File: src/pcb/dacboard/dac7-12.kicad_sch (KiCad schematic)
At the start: 18 parts, among them U22 AD8676xR, U23 AD8676xR, U24 AD8676xR, U25 AD8676xR, U26 AD5791BRUZ, U27 AD5791BRUZ, U28 AD5791BRUZ, U29 AD5791BRUZ, U30 AD8676xR, U31 AD8676xR, U32 AD5791BRUZ, U33 AD5791BRUZ

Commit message: dacboard routing
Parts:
- C28, C29, C30, C31, C32, C33: footprint (none) -> Capacitor_SMD:C_0603_1608Metric_Pad1.08x0.95mm_HandSolder
- U26, U27, U28, U29, U32, U33: footprint RU_20_ADI -> Package_SO:TSSOP-20_4.4x6.5mm_P0.65mm

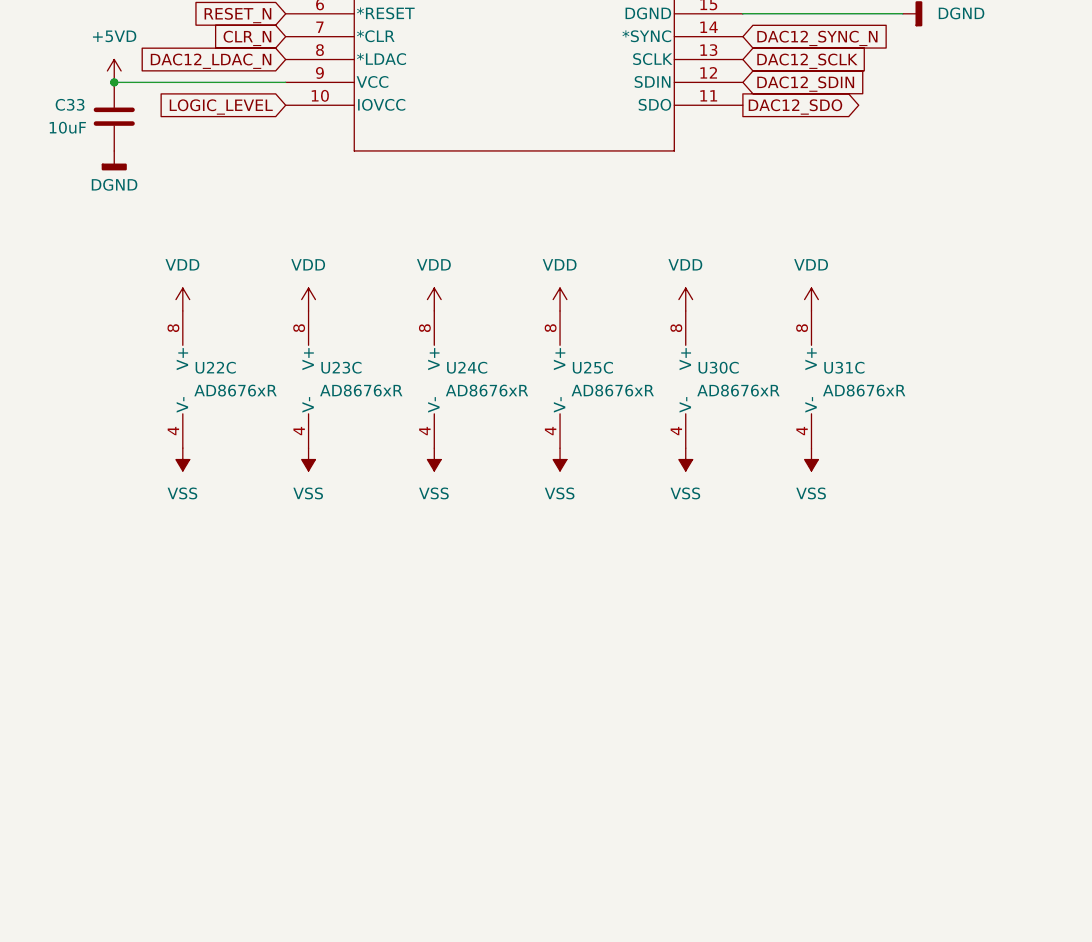
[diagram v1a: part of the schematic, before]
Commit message: adding more capacitors to analog side
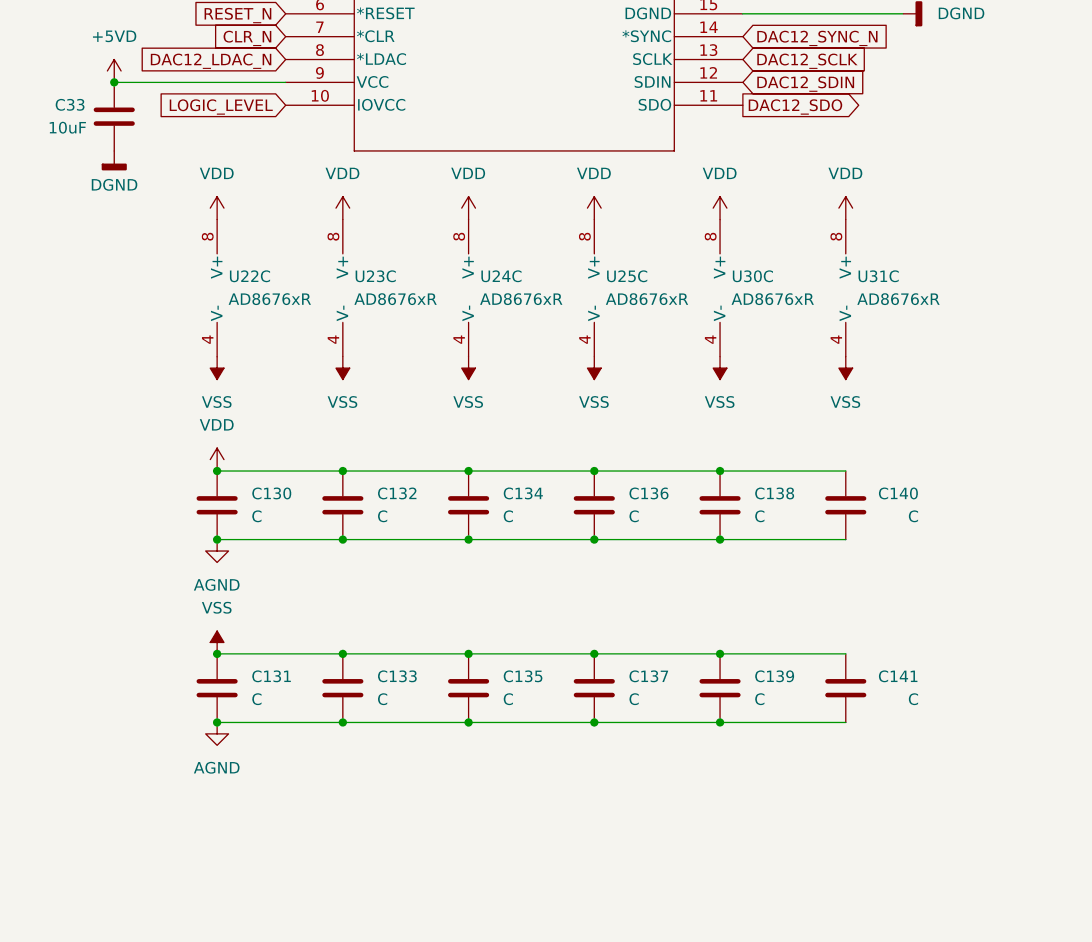
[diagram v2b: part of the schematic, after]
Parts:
- added C130, C131, C132, C133, C134, C135, C136, C137, C138, C139, C140, C141: C, Capacitor_SMD:C_0402_1005Metric_Pad0.74x0.62mm_HandSolder, symbol Device:C
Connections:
- net AGND: now also C130.2, C131.2, C132.2, C133.2, C134.2, C135.2, C136.2, C137.2, C138.2, C139.2, C140.2, C141.2
- net VDD: now also C130.1, C132.1, C134.1, C136.1, C138.1, C140.1
- net VSS: now also C131.1, C133.1, C135.1, C137.1, C139.1, C141.1
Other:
- moved on the sheet: U22C, U23C, U24C, U25C, U30C, U31C

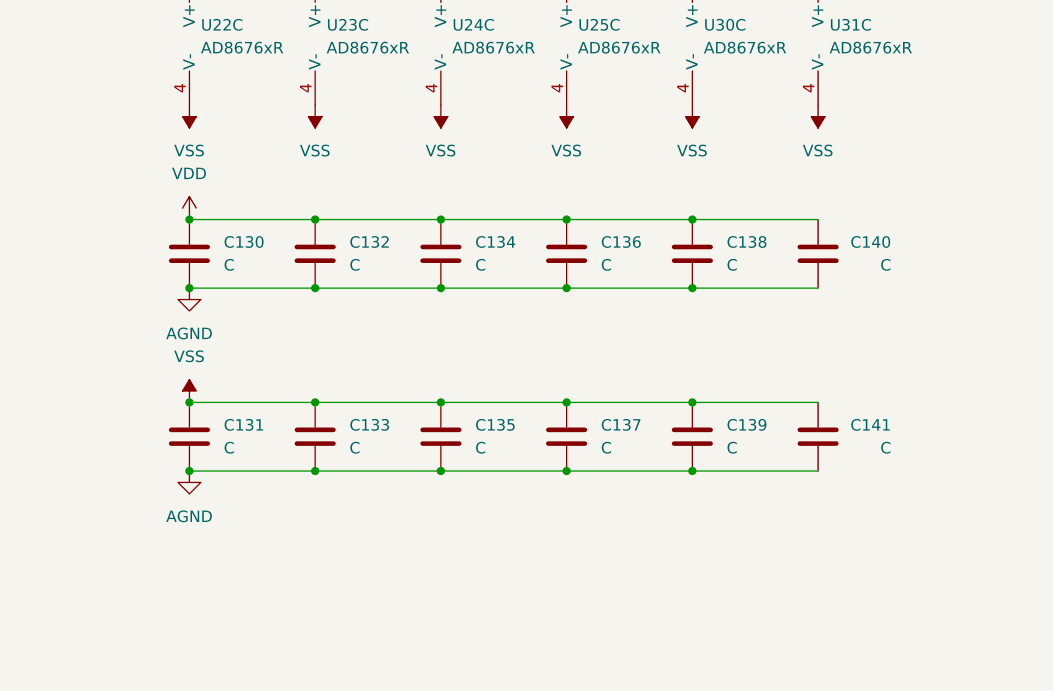
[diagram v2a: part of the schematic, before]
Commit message: more capacitors
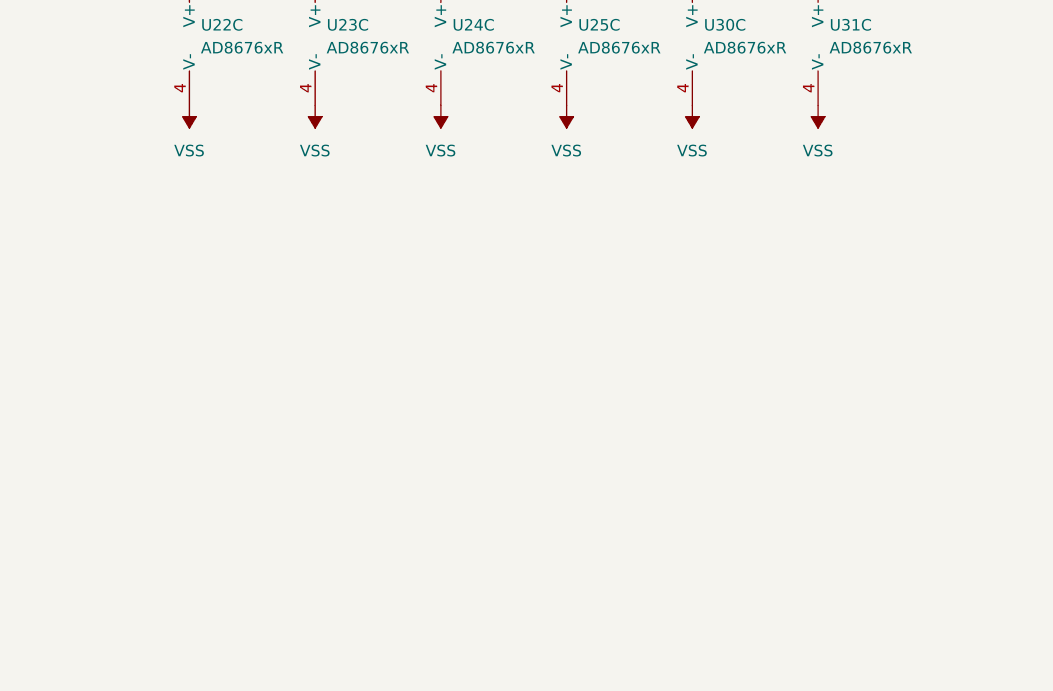
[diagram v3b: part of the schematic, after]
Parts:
- removed C130, C131, C132, C133, C134, C135, C136, C137, C138, C139, C140, C141: C, Capacitor_SMD:C_0402_1005Metric_Pad0.74x0.62mm_HandSolder, symbol Device:C

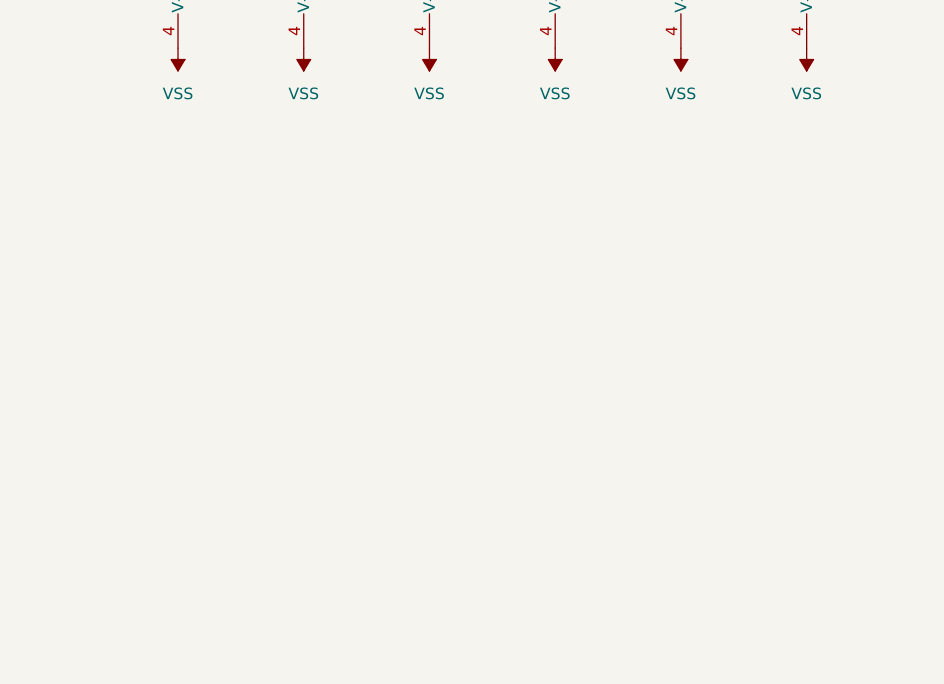
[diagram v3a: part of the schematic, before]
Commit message: got rid of all drc errors
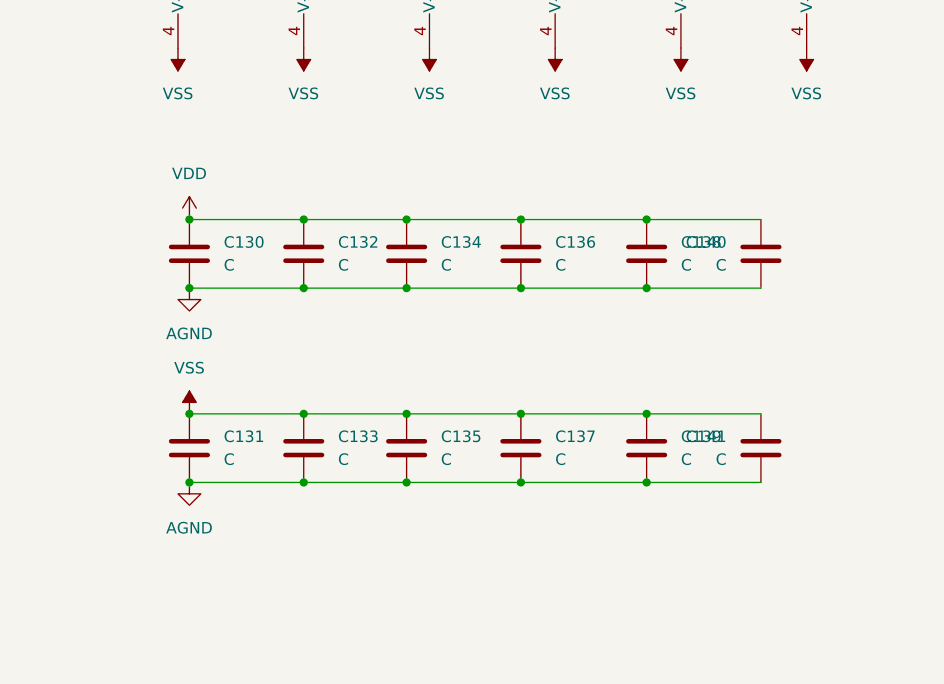
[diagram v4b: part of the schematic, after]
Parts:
- added C130, C131, C132, C133, C134, C135, C136, C137, C138, C139, C140, C141: C, Capacitor_SMD:C_0402_1005Metric_Pad0.74x0.62mm_HandSolder, symbol Device:C
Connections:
- net AGND: now also C130.2, C131.2, C132.2, C133.2, C134.2, C135.2, C136.2, C137.2, C138.2, C139.2, C140.2, C141.2
- net VDD: now also C130.1, C132.1, C134.1, C136.1, C138.1, C140.1
- net VSS: now also C131.1, C133.1, C135.1, C137.1, C139.1, C141.1
